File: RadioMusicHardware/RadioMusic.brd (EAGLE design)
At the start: 100 x 49 mm, 58 parts, among them IC1 TL074P, IC2 7805L

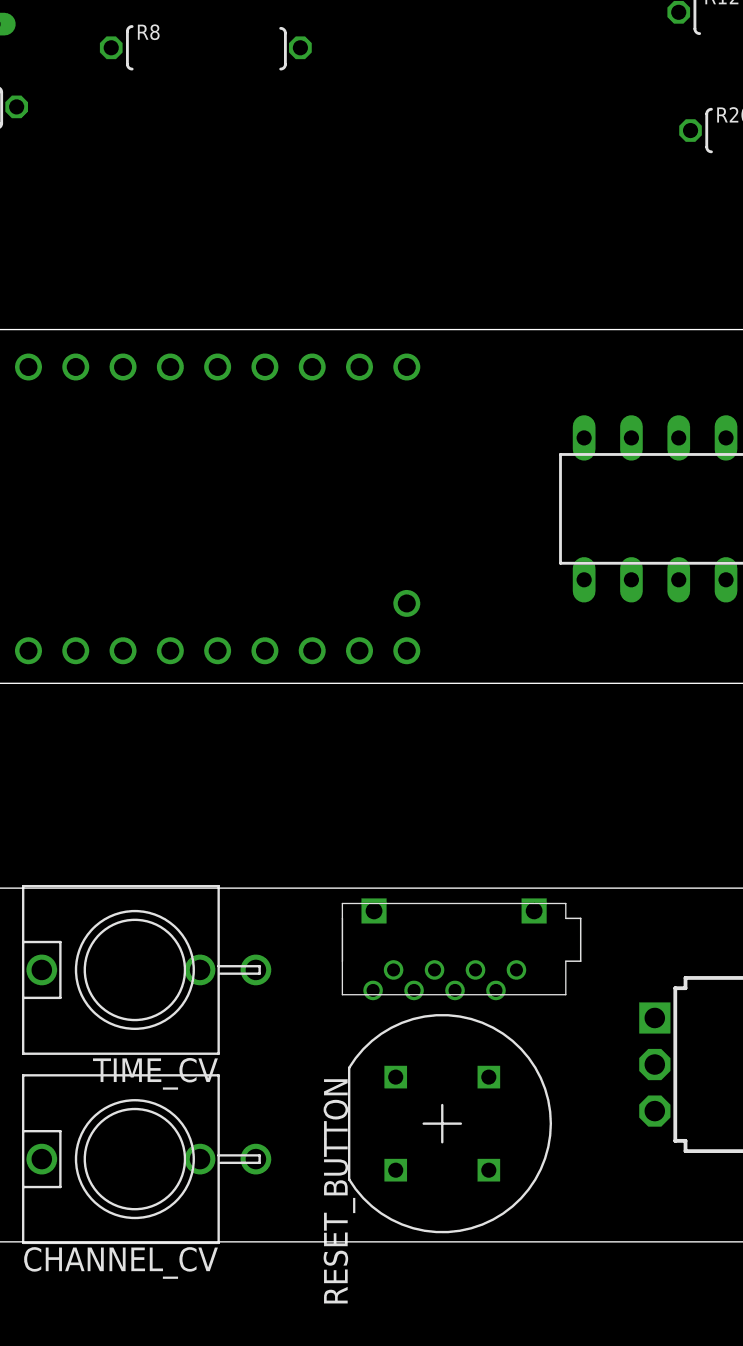
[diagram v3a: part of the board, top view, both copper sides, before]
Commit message: Added collateral folder
Replace these files in the Teensy Audio Library
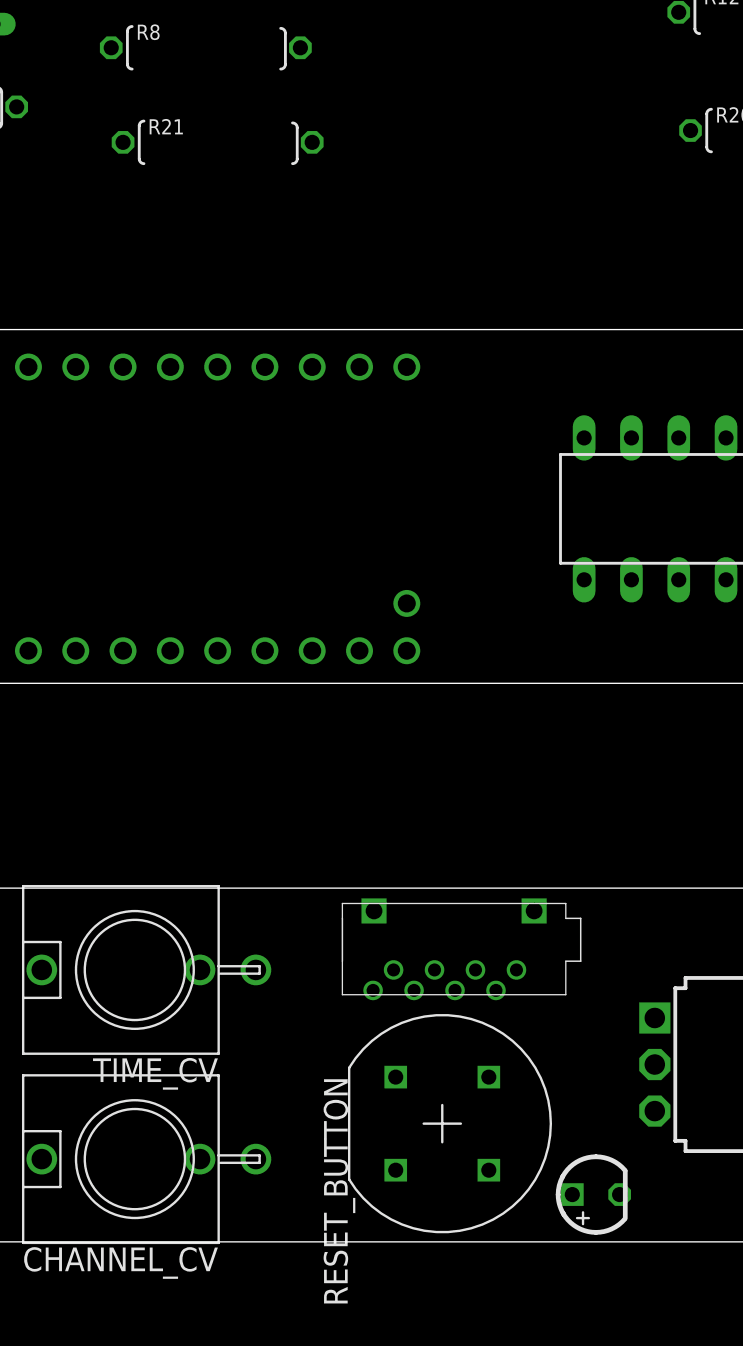
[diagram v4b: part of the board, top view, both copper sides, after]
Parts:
- added R21: 1k, TomW:0207/10
- added RESET_LED: (no value), TomW:LED3MM
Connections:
- new net N$24: RESET_LED.A, U$1.11
- new net N$25: R21.2, RESET_LED.K
- net GND: now also R21.1
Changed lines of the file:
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@@
 <element name="L1" library="inductors" package="BL01RN1A" value="BL01RN1A" x="84.455" y="45.085"/>
 <element name="L2" library="inductors" package="BL01RN1A" value="BL01RN1A" x="84.455" y="33.655"/>
+<element name="RESET_LED" library="TomW" package="LED3MM" value="" x="45.72" y="2.54"/>
+<element name="R21" library="TomW" package="0207/10" value="1k" x="25.4" y="59.055"/>
 </elements>
 <signals>
@@
 <contactref element="U$3" pad="P$6"/>
 <contactref element="U$1" pad="GND"/>
-<wire x1="92.71" y1="40.64" x2="95.25" y2="40.64" width="0" layer="19" extent="1-1"/>
+<contactref element="R21" pad="1"/>
+<wire x1="73.66" y1="73.66" x2="75.565" y2="86.36" width="0" layer="19" extent="1-1"/>
+<wire x1="71.12" y1="74.295" x2="73.66" y2="73.66" width="0" layer="19" extent="1-1"/>
+<wire x1="75.565" y1="64.77" x2="73.66" y2="73.66" width="0" layer="19" extent="1-1"/>
+<wire x1="75.565" y1="60.96" x2="75.565" y2="64.77" width="0" layer="19" extent="1-1"/>
+<wire x1="75.565" y1="57.15" x2="75.565" y2="60.96" width="0" layer="19" extent="1-1"/>
+<wire x1="70.485" y1="53.975" x2="75.565" y2="57.15" width="0" layer="19" extent="1-1"/>
+<wire x1="67.31" y1="60.325" x2="70.485" y2="53.975" width="0" layer="19" extent="1-1"/>
+<wire x1="73.66" y1="46.355" x2="70.485" y2="53.975" width="0" layer="19" extent="1-1"/>
+<wire x1="62.865" y1="69.85" x2="71.12" y2="74.295" width="0" layer="19" extent="1-1"/>
+<wire x1="83.82" y1="39.37" x2="73.66" y2="46.355" width="0" layer="19" extent="1-1"/>
+<wire x1="90.17" y1="40.64" x2="83.82" y2="39.37" width="0" layer="19" extent="1-1"/>
+<wire x1="92.71" y1="40.64" x2="90.17" y2="40.64" width="0" layer="19" extent="1-1"/>
+<wire x1="95.25" y1="40.64" x2="92.71" y2="40.64" width="0" layer="19" extent="1-1"/>
 <wire x1="95.25" y1="38.1" x2="95.25" y2="40.64" width="0" layer="19" extent="1-1"/>
-<wire x1="90.17" y1="40.64" x2="92.71" y2="40.64" width="0" layer="19" extent="1-1"/>
 <wire x1="92.71" y1="38.1" x2="92.71" y2="40.64" width="0" layer="19" extent="1-1"/>
 <wire x1="90.17" y1="38.1" x2="90.17" y2="40.64" width="0" layer="19" extent="1-1"/>
-<wire x1="83.82" y1="39.37" x2="90.17" y2="40.64" width="0" layer="19" extent="1-1"/>
+<wire x1="88.265" y1="31.75" x2="90.17" y2="38.1" width="0" layer="19" extent="1-1"/>
 <wire x1="88.265" y1="47.625" x2="90.17" y2="40.64" width="0" layer="19" extent="1-1"/>
-<wire x1="73.66" y1="46.355" x2="88.265" y2="47.625" width="0" layer="19" extent="1-1"/>
-<wire x1="88.265" y1="31.75" x2="90.17" y2="38.1" width="0" layer="19" extent="1-1"/>
-<wire x1="73.66" y1="32.385" x2="88.265" y2="31.75" width="0" layer="19" extent="1-1"/>
-<wire x1="75.565" y1="57.15" x2="73.66" y2="32.385" width="0" layer="19" extent="1-1"/>
-<wire x1="75.565" y1="60.96" x2="75.565" y2="57.15" width="0" layer="19" extent="1-1"/>
-<wire x1="75.565" y1="64.77" x2="75.565" y2="60.96" width="0" layer="19" extent="1-1"/>
-<wire x1="70.485" y1="53.975" x2="75.565" y2="57.15" width="0" layer="19" extent="1-1"/>
-<wire x1="67.31" y1="60.325" x2="70.485" y2="53.975" width="0" layer="19" extent="1-1"/>
-<wire x1="73.66" y1="73.66" x2="75.565" y2="64.77" width="0" layer="19" extent="1-1"/>
-<wire x1="71.12" y1="74.295" x2="73.66" y2="73.66" width="0" layer="19" extent="1-1"/>
-<wire x1="62.865" y1="69.85" x2="71.12" y2="74.295" width="0" layer="19" extent="1-1"/>
-<wire x1="75.565" y1="86.36" x2="73.66" y2="73.66" width="0" layer="19" extent="1-1"/>
+<wire x1="73.66" y1="32.385" x2="83.82" y2="39.37" width="0" layer="19" extent="1-1"/>
 <wire x1="50.8" y1="59.69" x2="62.865" y2="69.85" width="0" layer="19" extent="1-1"/>
 <wire x1="40.64" y1="75.565" x2="50.8" y2="59.69" width="0" layer="19" extent="1-1"/>
@@
 <wire x1="13.335" y1="65.405" x2="19.685" y2="67.945" width="0" layer="19" extent="1-1"/>
 <wire x1="4.445" y1="76.835" x2="13.335" y2="65.405" width="0" layer="19" extent="1-1"/>
-<wire x1="2.54" y1="46.99" x2="50.8" y2="59.69" width="0" layer="19" extent="1-1"/>
-<wire x1="33.8" y1="17.775" x2="2.54" y2="46.99" width="0" layer="19" extent="1-1"/>
-<wire x1="35.95" y1="13.505" x2="33.8" y2="17.775" width="0" layer="19" extent="1-1"/>
+<wire x1="2.54" y1="46.99" x2="13.335" y2="65.405" width="0" layer="19" extent="1-1"/>
+<wire x1="76.82" y1="7.025" x2="73.66" y2="32.385" width="0" layer="19" extent="1-1"/>
+<wire x1="48.88" y1="12.025" x2="76.82" y2="7.025" width="0" layer="19" extent="1-1"/>
+<wire x1="42.4" y1="17.775" x2="48.88" y2="12.025" width="0" layer="19" extent="1-1"/>
+<wire x1="35.95" y1="13.505" x2="42.4" y2="17.775" width="0" layer="19" extent="1-1"/>
+<wire x1="33.8" y1="17.775" x2="35.95" y2="13.505" width="0" layer="19" extent="1-1"/>
 <wire x1="27.455" y1="14.605" x2="33.8" y2="17.775" width="0" layer="19" extent="1-1"/>
-<wire x1="42.4" y1="17.775" x2="35.95" y2="13.505" width="0" layer="19" extent="1-1"/>
-<wire x1="48.88" y1="12.025" x2="42.4" y2="17.775" width="0" layer="19" extent="1-1"/>
 <wire x1="27.455" y1="4.445" x2="27.455" y2="14.605" width="0" layer="19" extent="1-1"/>
 <wire x1="12.85" y1="14.605" x2="27.455" y2="14.605" width="0" layer="19" extent="1-1"/>
 <wire x1="12.85" y1="4.445" x2="12.85" y2="14.605" width="0" layer="19" extent="1-1"/>
-<wire x1="76.82" y1="7.025" x2="48.88" y2="12.025" width="0" layer="19" extent="1-1"/>
+<wire x1="20.32" y1="59.055" x2="12.85" y2="4.445" width="0" layer="19" extent="1-1"/>
 </signal>
 <signal name="+12V" class="1">
@@
 <wire x1="79.375" y1="33.655" x2="93.345" y2="45.085" width="0" layer="19" extent="1-1"/>
 </signal>
+<signal name="N$24">
+<contactref element="U$1" pad="11"/>
+<contactref element="RESET_LED" pad="A"/>
+<wire x1="44.45" y1="2.54" x2="33.02" y2="46.99" width="0" layer="19" extent="1-1"/>
+</signal>
+<signal name="N$25">
+<contactref element="RESET_LED" pad="K"/>
+<contactref element="R21" pad="2"/>
+<wire x1="30.48" y1="59.055" x2="46.99" y2="2.54" width="0" layer="19" extent="1-1"/>
+</signal>
 </signals>

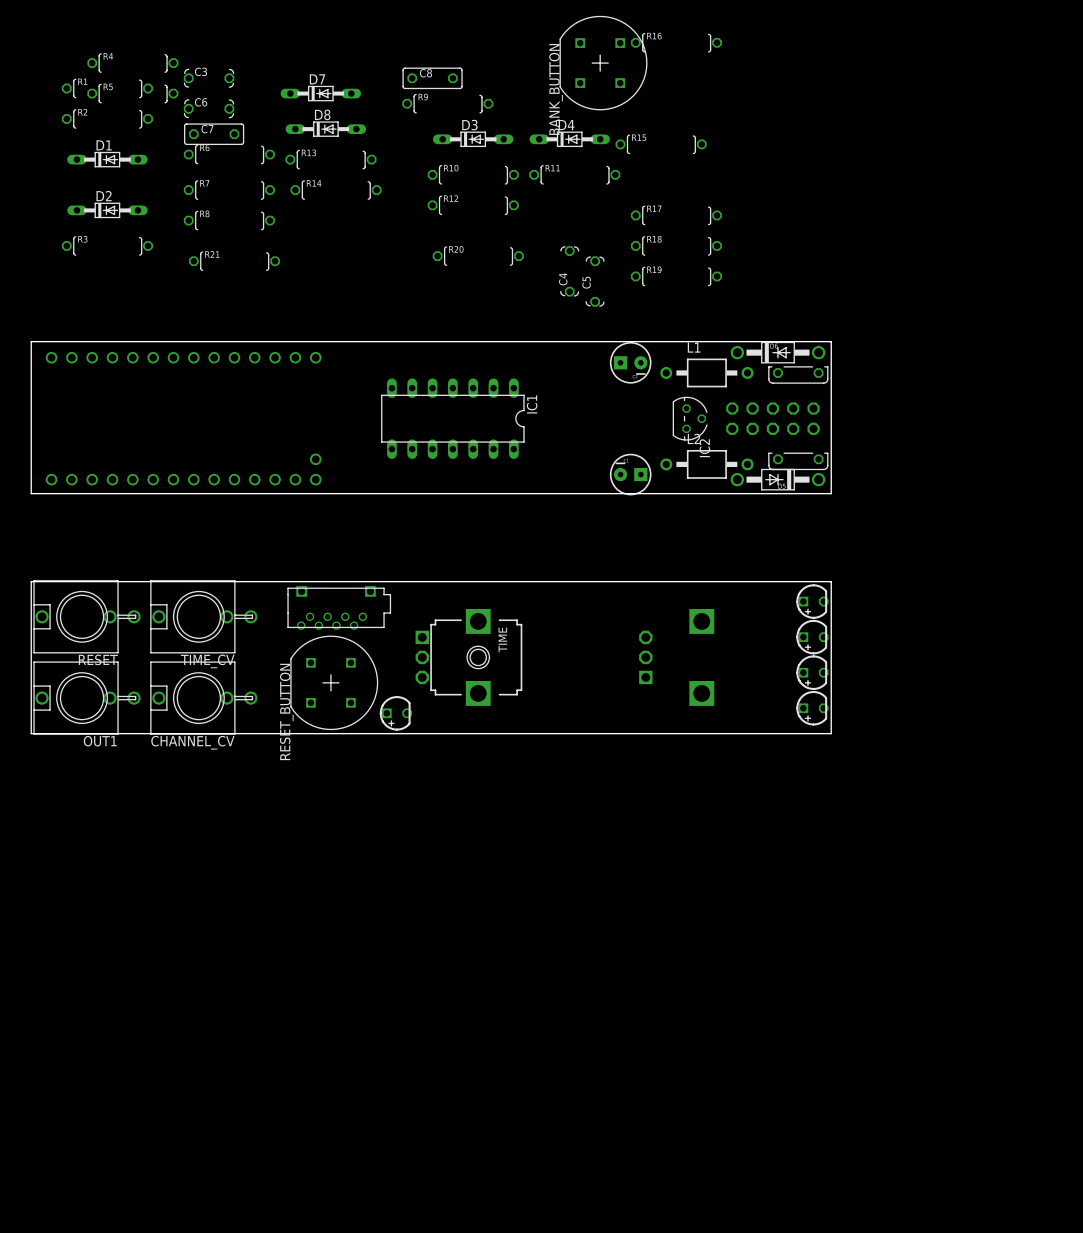
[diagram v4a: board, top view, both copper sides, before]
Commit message: Untested fade circuit + more PCB layout
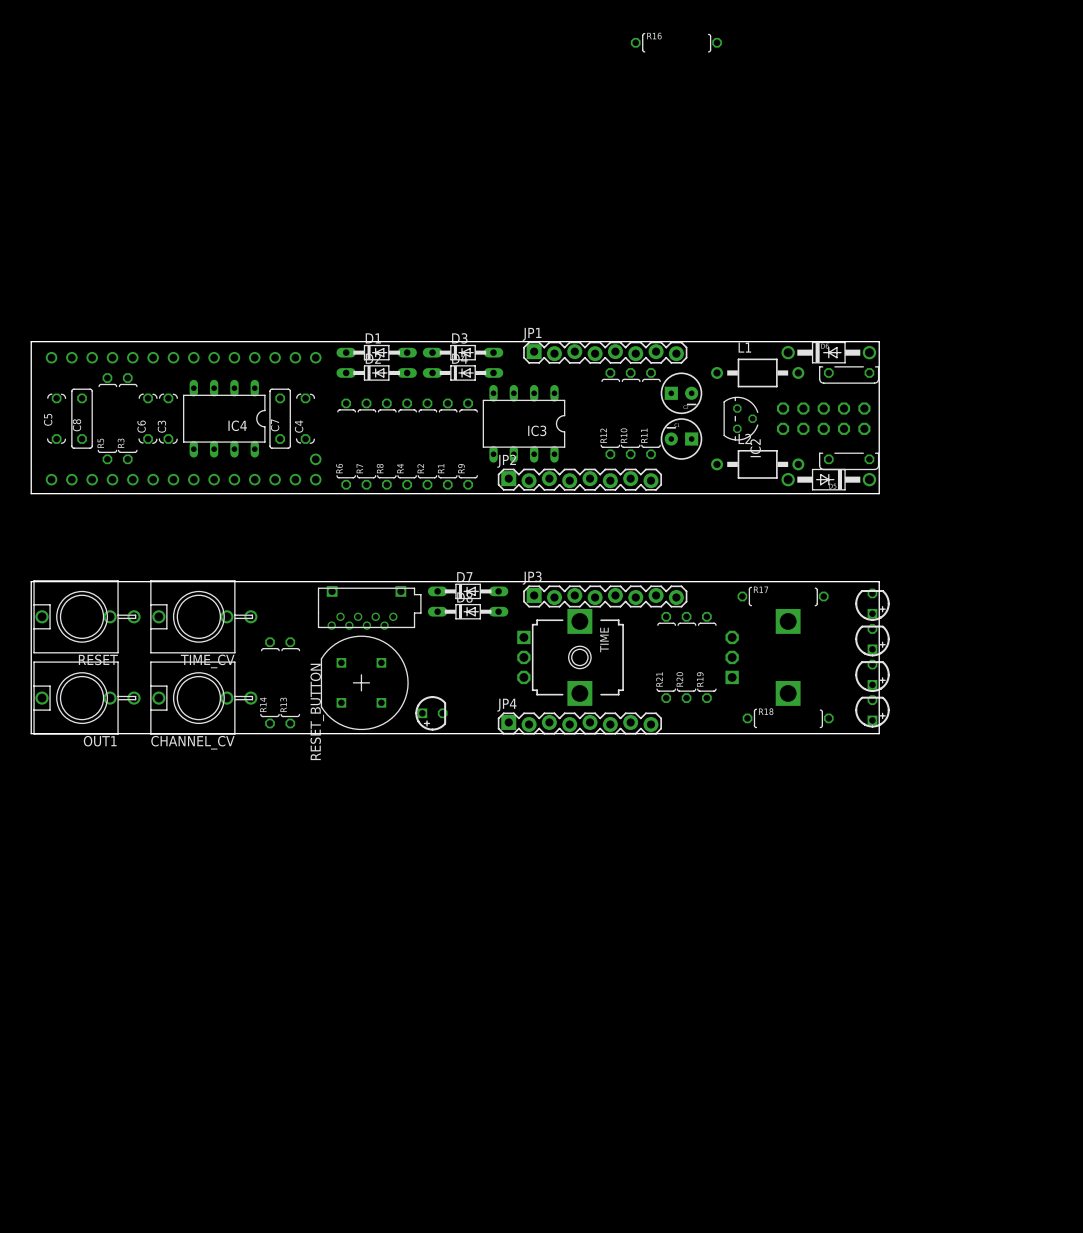
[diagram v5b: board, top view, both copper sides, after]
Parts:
- removed BANK_BUTTON: D6_PUSH_SWITCH, TomW:D6_BUTTON_RND
- removed IC1: TL074P, linear:DIL14
- removed R15: 10k, TomW:0207/10
- added IC3, IC4: TL072P, TomW:DIL08
- added JP1, JP2, JP3, JP4: (no value), SparkFun-Connectors:1X08_LOCK
- R6: value 8.2k -> 330K
- moved R21 73.3 mm to (79.4, 9.53), turned to 90 degrees
- moved C5 69.5 mm to (3.17, 39.4)
- moved R13 65.6 mm to (32.4, 6.35), turned to 90 degrees
- moved D7 64.9 mm to (54.6, 17.8)
- moved D8 62.9 mm to (54.6, 15.2)
- moved R14 62.1 mm to (29.8, 6.35), turned to 90 degrees
- moved R1 61.5 mm to (52.1, 36.2), turned to 90 degrees
- moved C8 61.1 mm to (6.35, 39.4), turned to 90 degrees
- moved R18 60.7 mm to (94.6, 1.91)
- moved R4 58.7 mm to (47.0, 36.2), turned to 90 degrees
- moved R2 57.0 mm to (49.5, 36.2), turned to 90 degrees
- moved R20 56.5 mm to (81.9, 9.53), turned to 90 degrees
- moved R17 49.5 mm to (94.0, 17.1)
- moved R19 47.8 mm to (84.5, 9.53), turned to 90 degrees
- moved C3 42.8 mm to (17.1, 39.4), turned to 90 degrees
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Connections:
- net +3.3V: no longer BANK_BUTTON.P$3, BANK_BUTTON.P$4
- net GND: no longer R15.1
- net N$12: now also IC3.5; no longer IC1.5
- net N$2: now also IC4.3; no longer IC1.10
- net N$3: now also IC3.3; no longer IC1.3
- net N$5: now also IC4.1, IC4.2; no longer IC1.8, IC1.9
- net N$6: now also IC4.5; no longer IC1.12
- net N$7: now also IC4.6; no longer IC1.13
- net N$8: now also IC4.7; no longer IC1.14
- net PIN2: no longer BANK_BUTTON.P$1, BANK_BUTTON.P$2, R15.2
- net PIN22/A8: now also IC3.1, IC3.2, IC3.6, IC3.7; no longer IC1.1, IC1.2, IC1.6, IC1.7
- net V+: now also IC3.8, IC4.8; no longer IC1.4
- net V-: now also IC3.4, IC4.4; no longer IC1.11
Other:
- board size 100 x 49 mm -> 106 x 49 mm

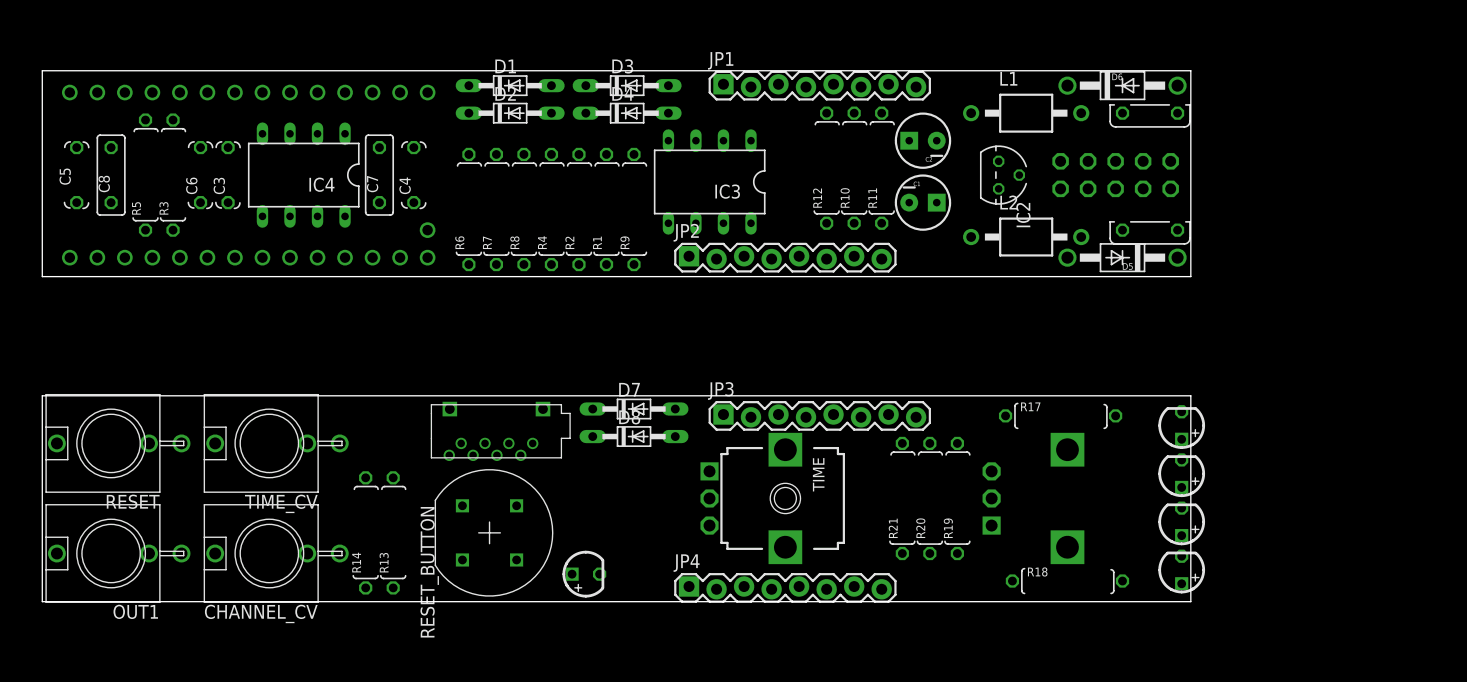
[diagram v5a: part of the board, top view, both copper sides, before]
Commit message: Power to op amps!
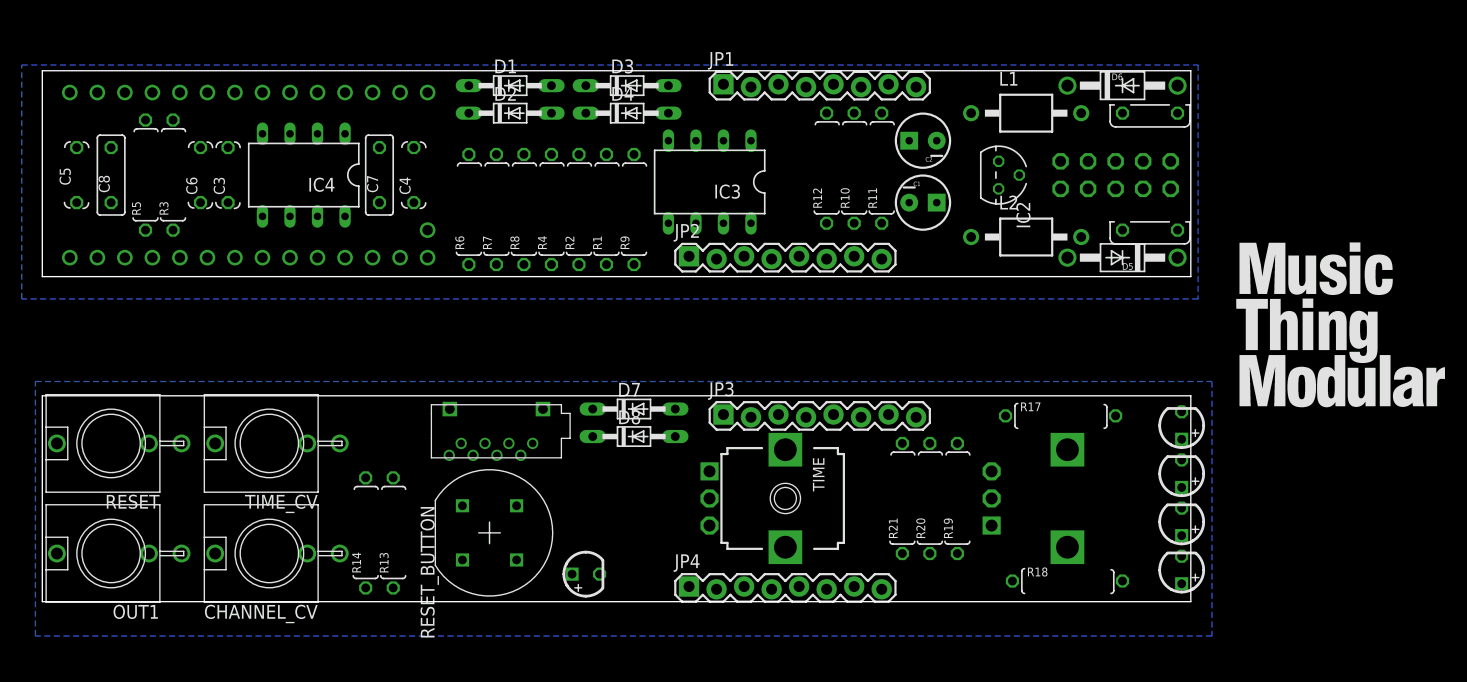
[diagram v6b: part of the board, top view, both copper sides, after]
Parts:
- moved U$2 22.2 mm to (110.5, 18.0), flipped to the top, turned to 0 degrees
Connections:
- removed net V+: IC3.8, IC4.8
- removed net V-: IC3.4, IC4.4
- net +12V: now also IC3.8, IC4.8
- net -12V: now also IC3.4, IC4.4
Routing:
- added copper zone on layer 16, net GND
